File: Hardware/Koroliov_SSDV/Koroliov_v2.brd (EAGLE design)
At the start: 56.8 x 80 mm, 24 parts

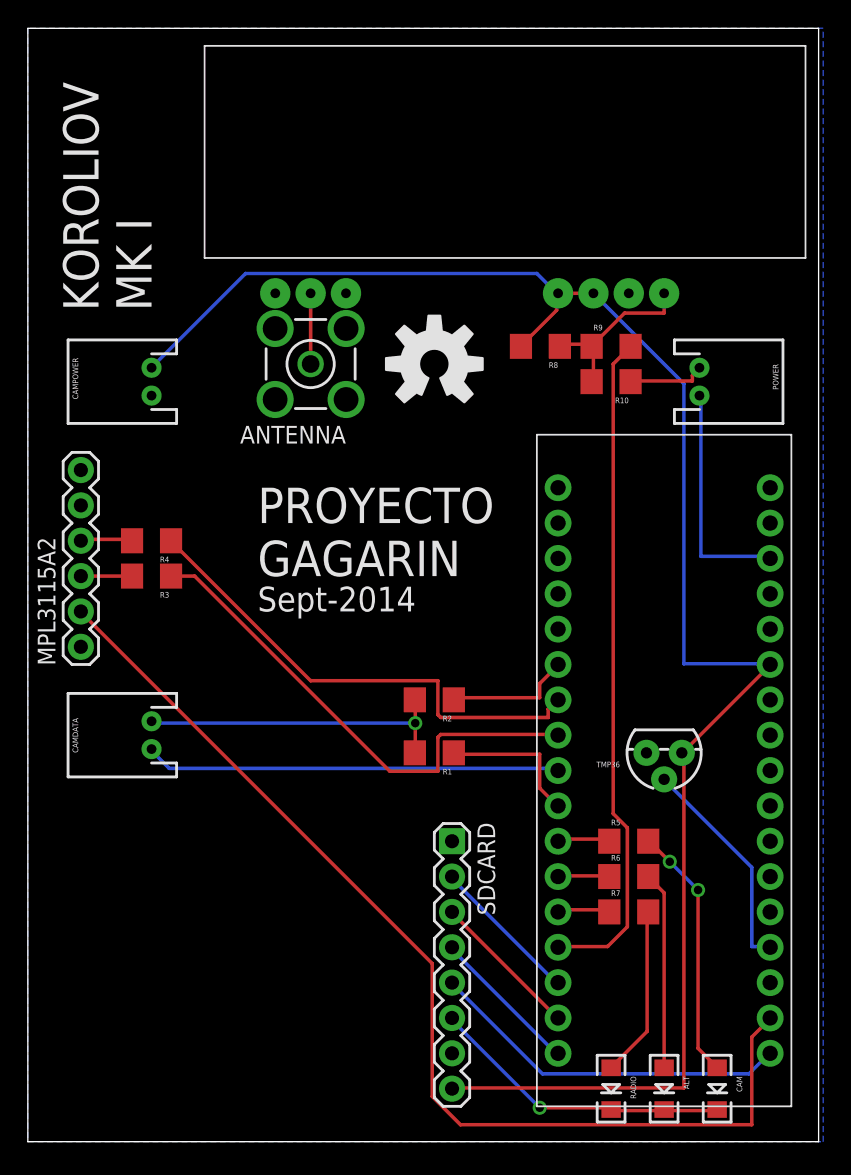
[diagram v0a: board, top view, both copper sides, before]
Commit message: Fixes after first fabrication
Arduino Micro was not fully compatible with previous layout for the
camera and the SD card. Antenna SMA connector has been moved to edge for
better connection with antenna cable.
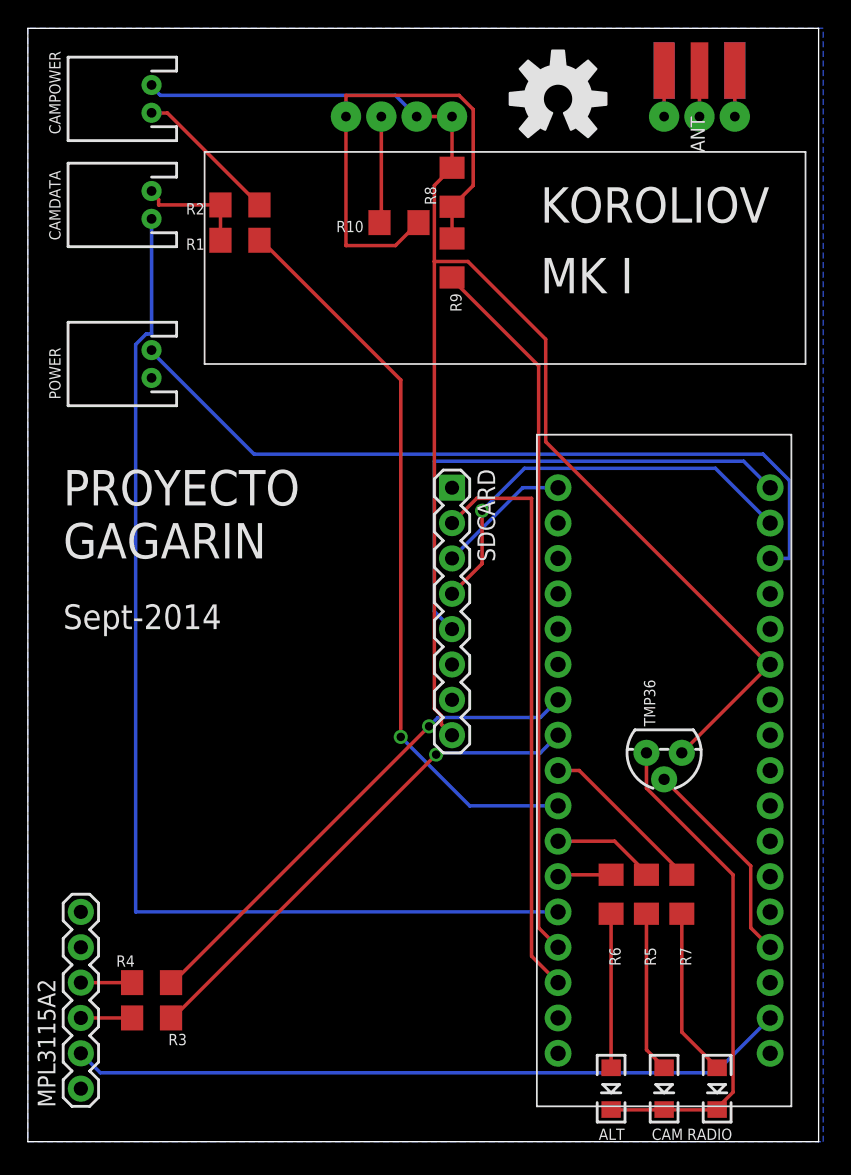
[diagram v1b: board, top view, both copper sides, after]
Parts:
- removed ANTENNA: BU-SMA-V, con-coax:BU-SMA-V
- added ANT: (no value), adafruit:SMA_EDGELAUNCH
- moved R1 39.4 mm to (15.2, 64.8)
- moved POWER 39.4 mm to (8.89, 55.9), turned to 90 degrees
- moved R2 38.2 mm to (15.2, 67.3)
- moved CAMDATA 38.1 mm to (8.89, 67.3)
- moved MPL3115A2 31.8 mm to (3.81, 3.81)
- moved R3 31.8 mm to (8.89, 8.89)
- moved R4 31.8 mm to (8.89, 11.4)
- moved SDCARD 25.4 mm to (30.5, 47.0)
- moved NTX2 24.1 mm to (22.9, 63.5), turned to 180 degrees
- moved LOGO1 21.0 mm to (38.1, 74.9)
- moved CAMPOWER 20.3 mm to (8.89, 74.9)
- moved R10 19.1 mm to (26.7, 66.0), turned to 0 degrees
- moved R9 13.1 mm to (30.5, 63.5), turned to 270 degrees
- moved R8 13.1 mm to (30.5, 68.6), turned to 90 degrees
- moved RADIO 7.62 mm to (49.5, 3.81)
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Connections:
- new net STATUS_SD: ARDUINOMICRO.P$34
- net CAMTX: now also ARDUINOMICRO.P$5; no longer ARDUINOMICRO.P$9
- net GND: now also ANT.GND@1, ANT.GND@2, ANT.GND@3, ANT.GND@4; no longer ANTENNA.2, ANTENNA.3, ANTENNA.4, ANTENNA.5
- net N$1: now also ANT.P; no longer ANTENNA.1
- net SDCLK: now also ARDUINOMICRO.P$18; no longer ARDUINOMICRO.P$34
- net SDDI: now also ARDUINOMICRO.P$17; no longer ARDUINOMICRO.P$2
- net SDDO: now also ARDUINOMICRO.P$19; no longer ARDUINOMICRO.P$1
- net STATUS_RADIO: now also ARDUINOMICRO.P$9; no longer ARDUINOMICRO.P$5
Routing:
- net CAMTX: track 29.9 -> 80.8 mm
- net ARDUINOTX: track 10.5 -> 53.3 mm, vias 0 -> 1
- net VIN: track 16.6 -> 56.8 mm
- net SDCS: track 10.9 -> 42.0 mm
- net 3.3V: track 77.3 -> 51.7 mm
- net GND: track 36.8 -> 61.2 mm, vias 1 -> 0
- net N$7: track 12.8 -> 36.2 mm
- net SDDO: track 10.9 -> 30.5 mm, vias 0 -> 1
- net CAMRX: track 22.9 -> 8.20 mm, vias 1 -> 0
- net SDCLK: track 26.2 -> 37.5 mm
- net STATUS_RADIO: track 3.83 -> 12.1 mm
- net 5V: track 125.5 -> 117.5 mm
- net N$2: track 18.4 -> 11.6 mm, vias 2 -> 0
- net STATUS_CAMERA: track 3.83 -> 7.42 mm
- net N$3: track 14.2 -> 11.1 mm
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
